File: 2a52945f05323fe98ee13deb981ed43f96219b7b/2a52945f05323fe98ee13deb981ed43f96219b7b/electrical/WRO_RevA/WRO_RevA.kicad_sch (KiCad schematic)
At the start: 29 parts, among them J1 MPU6050, J1 VCC, J2 Conn_01x05_Pin, SW1 EXEC_PRGM, U1 ESP32-DEVKIT-V1, U2 ROB-14450

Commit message: schematic done
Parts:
- added J3: MOTOR, TerminalBlock_Phoenix:TerminalBlock_Phoenix_PT-1,5-2-5.0-H_1x02_P5.00mm_Horizontal, symbol Connector:Screw_Terminal_01x02
- added J4: SERVO, Connector_PinSocket_2.54mm:PinSocket_1x03_P2.54mm_Vertical, symbol Connector:Conn_01x03_Pin
- J2: value Conn_01x05_Pin -> TO_PI
- renumbered Reductor_corriente_3.3v1 to MINI560
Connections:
- net +5V: now also J4.2 (Pin_2); no longer SW1.1 (A)
- net ECHO1: now also U1.4 (D2)
- net ECHO2: now also U1.8 (D5)
- net ECHO3: now also U1.28 (D13)
- net ECHO4: now also U1.24 (D26)
- net GND: now also J4.1 (Pin_1)
- net TRIG1: now also U1.5 (D4)
- net TRIG2: now also U1.27 (D12)
- net TRIG3: now also U1.26 (D14)
- net TRIG4: now also U1.25 (D27)
- net STBY: now reaches U2.13 (STBY)
- net STBY: now also U1.23 (D25)
- net DIR_A: now reaches U2.14 (AI1)
- net DIR_A: now also U1.9 (D18)
- net DIR_B: now reaches U2.15 (AI2)
- net DIR_B: now also U1.10 (D19)
- net PWM_MOTOR: now reaches U2.16 (PWMA)
- net PWM_MOTOR: now also U1.15 (D23)
- net MOTOR_1: now reaches U2.4 (A01)
- net MOTOR_1: now also J3.2 (Pin_2)
- net MOTOR_2: now reaches U2.5 (A02)
- net MOTOR_2: now also J3.1 (Pin_1)
- net +3V3: now reaches U1.1 (3V3)
- net +3V3: now also SW1.1 (A)
- net SERVO: now reaches U1.3 (D15)
- net SERVO: now also J4.3 (Pin_3)
- no-connect marks 4 -> 18
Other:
- note added: "Connection Pins for MCU"
- note added: "ESP32"
- note added: "Excecute Button"
- note added: "Motor w/ Driver"
- note added: "Power Distribution"
- note added: "Status LEDs"
- moved on the sheet: C1, C2, C3, C4, C5, C6, D1, D2, J1, J2, MINI560, R1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

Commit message: added mods
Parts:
- C3: footprint (none) -> Capacitor_THT:CP_Radial_D5.0mm_P2.00mm
- J3: renamed from J2; footprint (none) -> Connector_PinHeader_2.54mm:PinHeader_1x05_P2.54mm_Vertical
- MINI560: footprint Mini560:Mini560 -> Libreria_mia:Mini560
- US1, US2, US3, US4: footprint (none) -> Connector_PinSocket_2.54mm:PinSocket_1x04_P2.54mm_Vertical
- renumbered J1 to J2, J3 to J5
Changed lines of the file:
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@@
 			)
 		)
-		(property "Footprint" ""
+		(property "Footprint" "Capacitor_THT:CP_Radial_D5.0mm_P2.00mm"
 			(at 134.3152 73.66 0)
 			(effects
@@
 		(dnp no)
 		(fields_autoplaced yes)
-		(property "Reference" "J1"
+		(property "Reference" "J2"
 			(at 193.04 109.2199 0)
 			(effects
@@
 			(project ""
 				(path "/737eb7c9-287d-4e9e-a07f-ac9efe008363"
-					(reference "J1")
+					(reference "J2")
 					(unit 1)
 				)
@@
 		(dnp no)
 		(fields_autoplaced yes)
-		(property "Reference" "J3"
+		(property "Reference" "J5"
 			(at 237.49 110.49 0)
 			(effects
@@
 			(project "WRO_RevA"
 				(path "/737eb7c9-287d-4e9e-a07f-ac9efe008363"
-					(reference "J3")
+					(reference "J5")
 					(unit 1)
 				)
@@
 			)
 		)
-		(property "Footprint" "Mini560:Mini560"
+		(property "Footprint" "Libreria_mia:Mini560"
 			(at 118.11 66.04 0)
 			(effects
@@
 			)
 		)
-		(property "Footprint" ""
+		(property "Footprint" "Connector_PinSocket_2.54mm:PinSocket_1x04_P2.54mm_Vertical"
 			(at 254 81.28 0)
 			(effects
@@
 			)
 		)
-		(property "Footprint" ""
+		(property "Footprint" "Connector_PinSocket_2.54mm:PinSocket_1x04_P2.54mm_Vertical"
 			(at 207.01 58.42 0)
 			(effects
@@
 			)
 		)
-		(property "Footprint" ""
+		(property "Footprint" "Connector_PinSocket_2.54mm:PinSocket_1x04_P2.54mm_Vertical"
 			(at 255.27 58.42 0)
 			(effects
@@
 			)
 		)
-		(property "Footprint" ""
+		(property "Footprint" "Connector_PinSocket_2.54mm:PinSocket_1x04_P2.54mm_Vertical"
 			(at 207.01 81.28 0)
 			(effects
@@
 		(dnp no)
 		(fields_autoplaced yes)
-		(property "Reference" "J2"
+		(property "Reference" "J3"
 			(at 223.52 105.4099 0)
 			(effects
@@
 			)
 		)
-		(property "Footprint" ""
+		(property "Footprint" "Connector_PinHeader_2.54mm:PinHeader_1x05_P2.54mm_Vertical"
 			(at 222.25 106.68 0)
 			(effects
@@
 			(project ""
 				(path "/737eb7c9-287d-4e9e-a07f-ac9efe008363"
-					(reference "J2")
+					(reference "J3")
 					(unit 1)
 				)

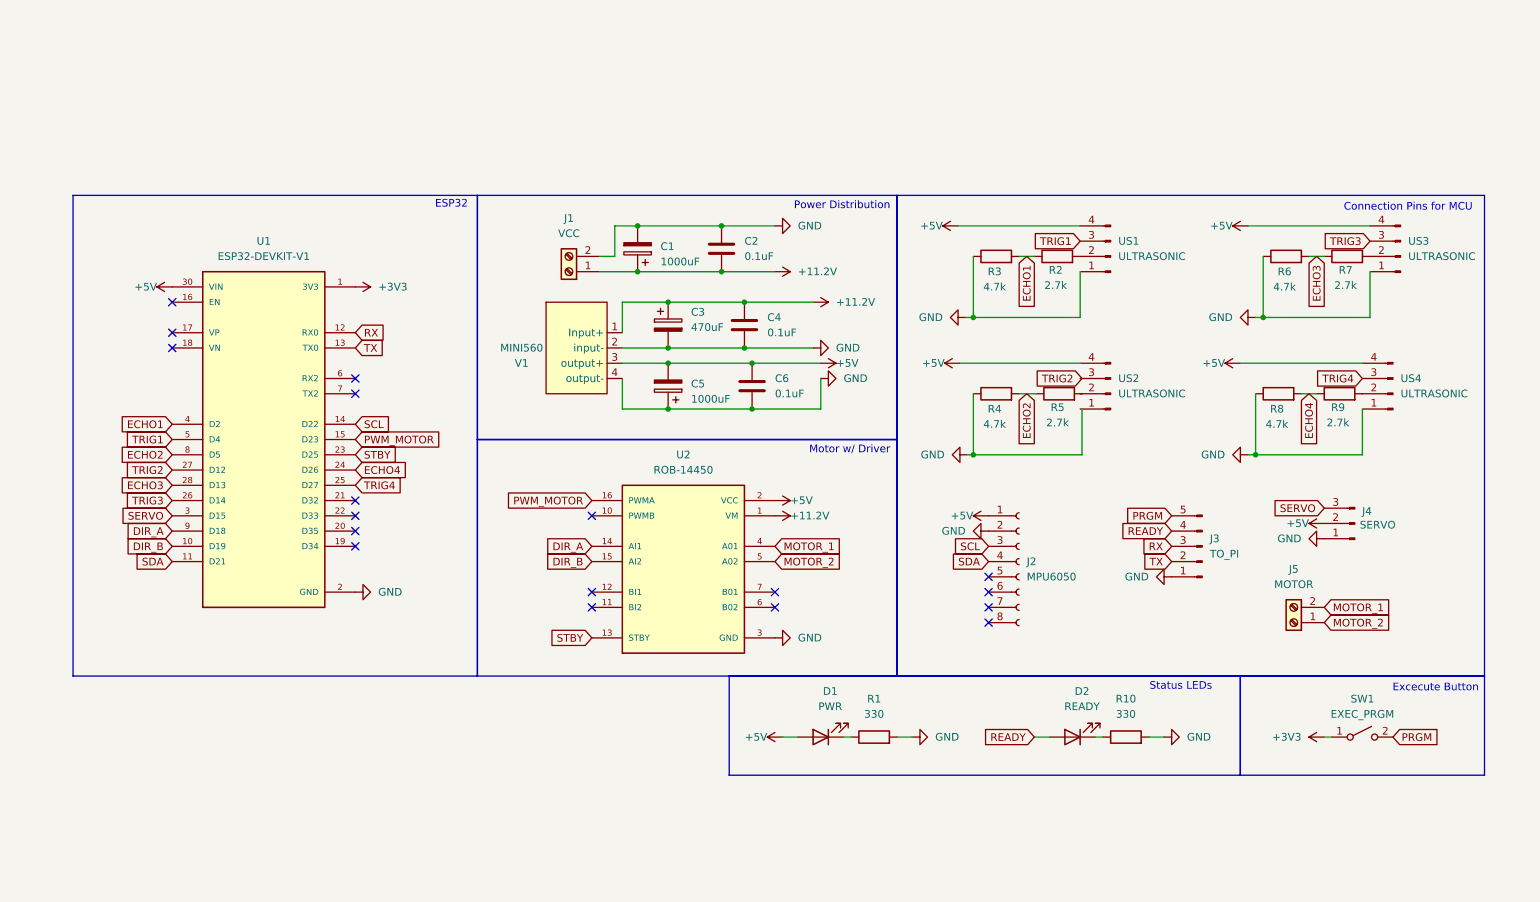
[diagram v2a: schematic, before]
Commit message: minor changes to PCB
Lvl shifter still too big. have to mod ultrasonics....
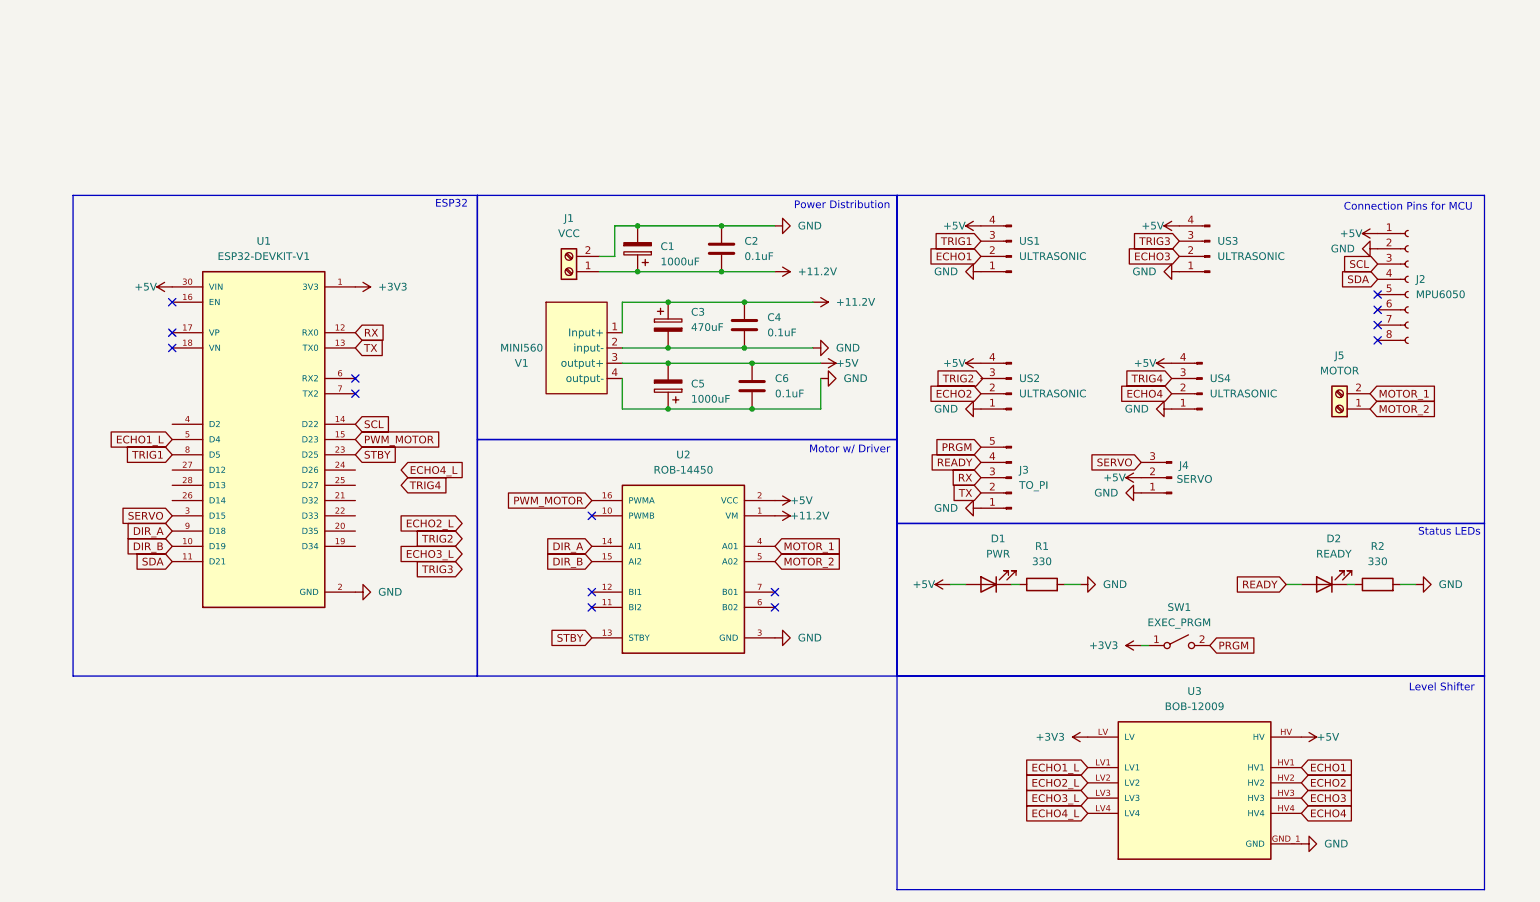
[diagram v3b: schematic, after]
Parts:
- removed R10: 330, Resistor_THT:R_Axial_DIN0309_L9.0mm_D3.2mm_P12.70mm_Horizontal, symbol Device:R
- removed R3, R4, R6, R8: 4.7k, Resistor_THT:R_Axial_DIN0207_L6.3mm_D2.5mm_P10.16mm_Horizontal, symbol Device:R
- removed R5, R7, R9: 2.7k, Resistor_THT:R_Axial_DIN0207_L6.3mm_D2.5mm_P10.16mm_Horizontal, symbol Device:R
- added U3: BOB-12009, Snapeda:CONV_BOB-12009, symbol Snapeda:BOB-12009
- R1: footprint Resistor_THT:R_Axial_DIN0309_L9.0mm_D3.2mm_P12.70mm_Horizontal -> Resistor_THT:R_Axial_DIN0204_L3.6mm_D1.6mm_P2.54mm_Vertical
- R2: value 2.7k -> 330; footprint Resistor_THT:R_Axial_DIN0207_L6.3mm_D2.5mm_P10.16mm_Horizontal -> Resistor_THT:R_Axial_DIN0204_L3.6mm_D1.6mm_P2.54mm_Vertical
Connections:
- net +3V3: now also U3.LV
- net +5V: now also U3.HV
- net ECHO1: now also US1.2 (Pin_2), U3.HV1; no longer R2.1, U1.4 (D2)
- net ECHO2: now also US2.2 (Pin_2), U3.HV2; no longer U1.8 (D5)
- net ECHO3: now also US3.2 (Pin_2), U3.HV3; no longer U1.28 (D13)
- net ECHO4: now also US4.2 (Pin_2), U3.HV4; no longer U1.24 (D26)
- net GND: now also R2.2, US2.1 (Pin_1), U3.GND_1 (GND), U3.GND_2 (GND)
- net TRIG1: now also U1.8 (D5); no longer U1.5 (D4)
- net TRIG2: no longer U1.27 (D12)
- net TRIG3: no longer U1.26 (D14)
- net TRIG4: no longer U1.25 (D27)
- net at D2.1 (K): now also R2.1
- new net ECHO1_L: U1.5 (D4), U3.LV1
- new net ECHO2_L: U3.LV2
- new net ECHO3_L: U3.LV3
- new net ECHO4_L: U3.LV4
- no-connect marks 18 -> 14
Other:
- note added: "Level Shifter"
- note removed: "Excecute Button"
- moved on the sheet: D1, D2, J2, J3, J4, J5, SW1, US1, US2, US3, US4

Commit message: minor changes
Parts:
- removed C3: 470uF, Capacitor_THT:CP_Radial_D5.0mm_P2.00mm, symbol Device:C_Polarized
- removed C4: 0.1uF, Capacitor_THT:C_Disc_D7.5mm_W2.5mm_P5.00mm, symbol Device:C
- removed U1: ESP32-DEVKIT-V1, Snapeda:MODULE_ESP32_DEVKIT_V1, symbol Snapeda:ESP32-DEVKIT-V1
- added U1: ESP32-DEVKITC-32D, ESP32-DEVKITC-32D:ESP32-DEVKITC-32D, symbol ESP32-DEVKITC-32D:ESP32-DEVKITC-32D
- C1: value 1000uF -> 470uF
- C3: renamed from C5; value 1000uF -> 470uF
- renumbered C6 to C4
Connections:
- net +3V3: now also U1.J2-1 (3V3)
- net +5V: now also C3.1, U1.J2-19 (EXT_5V); no longer C3.2
- net ECHO1_L: now also U1.J2-8 (IO33)
- net ECHO2_L: now also U1.J2-7 (IO32)
- net ECHO3_L: now also U1.J2-6 (IO35)
- net ECHO4_L: now also U1.J2-5 (IO34)
- net GND: now also C3.2, U1.J2-14 (GND1), U1.J3-1 (GND3), U1.J3-7 (GND2); no longer C3.1
- net PWM_MOTOR: now also U1.J3-2 (IO23)
- net RX: now also U1.J3-12 (IO16)
- net SCL: now also U1.J3-3 (IO22)
- net SDA: now also U1.J3-6 (IO21)
- net SERVO: now also U1.J2-15 (IO13)
- net STBY: now also U1.J2-13 (IO12)
- net TRIG1: now also U1.J2-12 (IO14)
- net TRIG2: now also U1.J2-11 (IO27)
- net TRIG3: now also U1.J2-10 (IO26)
- net TRIG4: now also U1.J2-9 (IO25)
- net TX: now also U1.J3-11 (IO17)
- net DIR_A renamed AIN1
- net AIN1: now also U1.J3-8 (IO19)
- net DIR_B renamed AIN2
- net AIN2: now also U1.J3-9 (IO18)
- no-connect marks 14 -> 24
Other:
- moved on the sheet: C3, J4

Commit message: final shape for PCB, only need to route
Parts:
- removed J2: MPU6050, Connector_PinSocket_2.54mm:PinSocket_1x08_P2.54mm_Vertical, symbol Connector:Conn_01x08_Socket
- added U4: MPU6050, usini_sensors:module_mpu6050, symbol usini_sensors:module_mpu6050
- US1, US2, US3, US4: footprint Connector_PinSocket_2.54mm:PinSocket_1x04_P2.54mm_Vertical -> Connector_PinHeader_2.54mm:PinHeader_1x04_P2.54mm_Vertical
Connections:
- net +5V: now also U4.1 (VCC)
- net GND: now also U4.2 (GND)
- net SCL: now also U4.3 (SCL)
- net SDA: now also U4.4 (SDA)
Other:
- moved on the sheet: J5

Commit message: started routing, added CREEA logo
gracias gustavo creea
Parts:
- C3: value 470uF -> 100uF
- J3: footprint Connector_PinHeader_2.54mm:PinHeader_1x05_P2.54mm_Vertical -> Connector_PinHeader_2.54mm:PinHeader_1x06_P2.54mm_Vertical; symbol Connector:Conn_01x05_Pin -> Connector:Conn_01x06_Pin
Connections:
- net +5V: now also J3.6 (Pin_6)
- net TRIG2: now also US2.3 (Pin_3)
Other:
- moved on the sheet: J4, J5, U4, US2, US4

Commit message: finished
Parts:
- added SW2: PWR, EasyEDA:SW-TH_L22.2-W15.0-P7.00_KCD1-2P-P, symbol EasyEDA:HXKCD1-2P-X
- J4: footprint Connector_PinSocket_2.54mm:PinSocket_1x03_P2.54mm_Vertical -> Connector_PinHeader_2.54mm:PinHeader_1x03_P2.54mm_Vertical
- R1, R2: footprint Resistor_THT:R_Axial_DIN0204_L3.6mm_D1.6mm_P2.54mm_Vertical -> Resistor_THT:R_Axial_DIN0204_L3.6mm_D1.6mm_P5.08mm_Horizontal
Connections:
- net +11.2V: now also SW2.2; no longer J1.1 (Pin_1)
- net +5V: now also U2.13 (STBY)
- net GND: now also J1.1 (Pin_1); no longer J1.2 (Pin_2)
- net STBY: no longer names the net of U1.J2-13 (IO12)
- net STBY: no longer U2.13 (STBY)
- new net: J1.2 (Pin_2), SW2.1
- no-connect marks 24 -> 26
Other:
- moved on the sheet: C1, C2
